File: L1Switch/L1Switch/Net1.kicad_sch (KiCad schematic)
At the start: 33 parts, among them J2 Conn_01x07_Male, U2 VSC8658

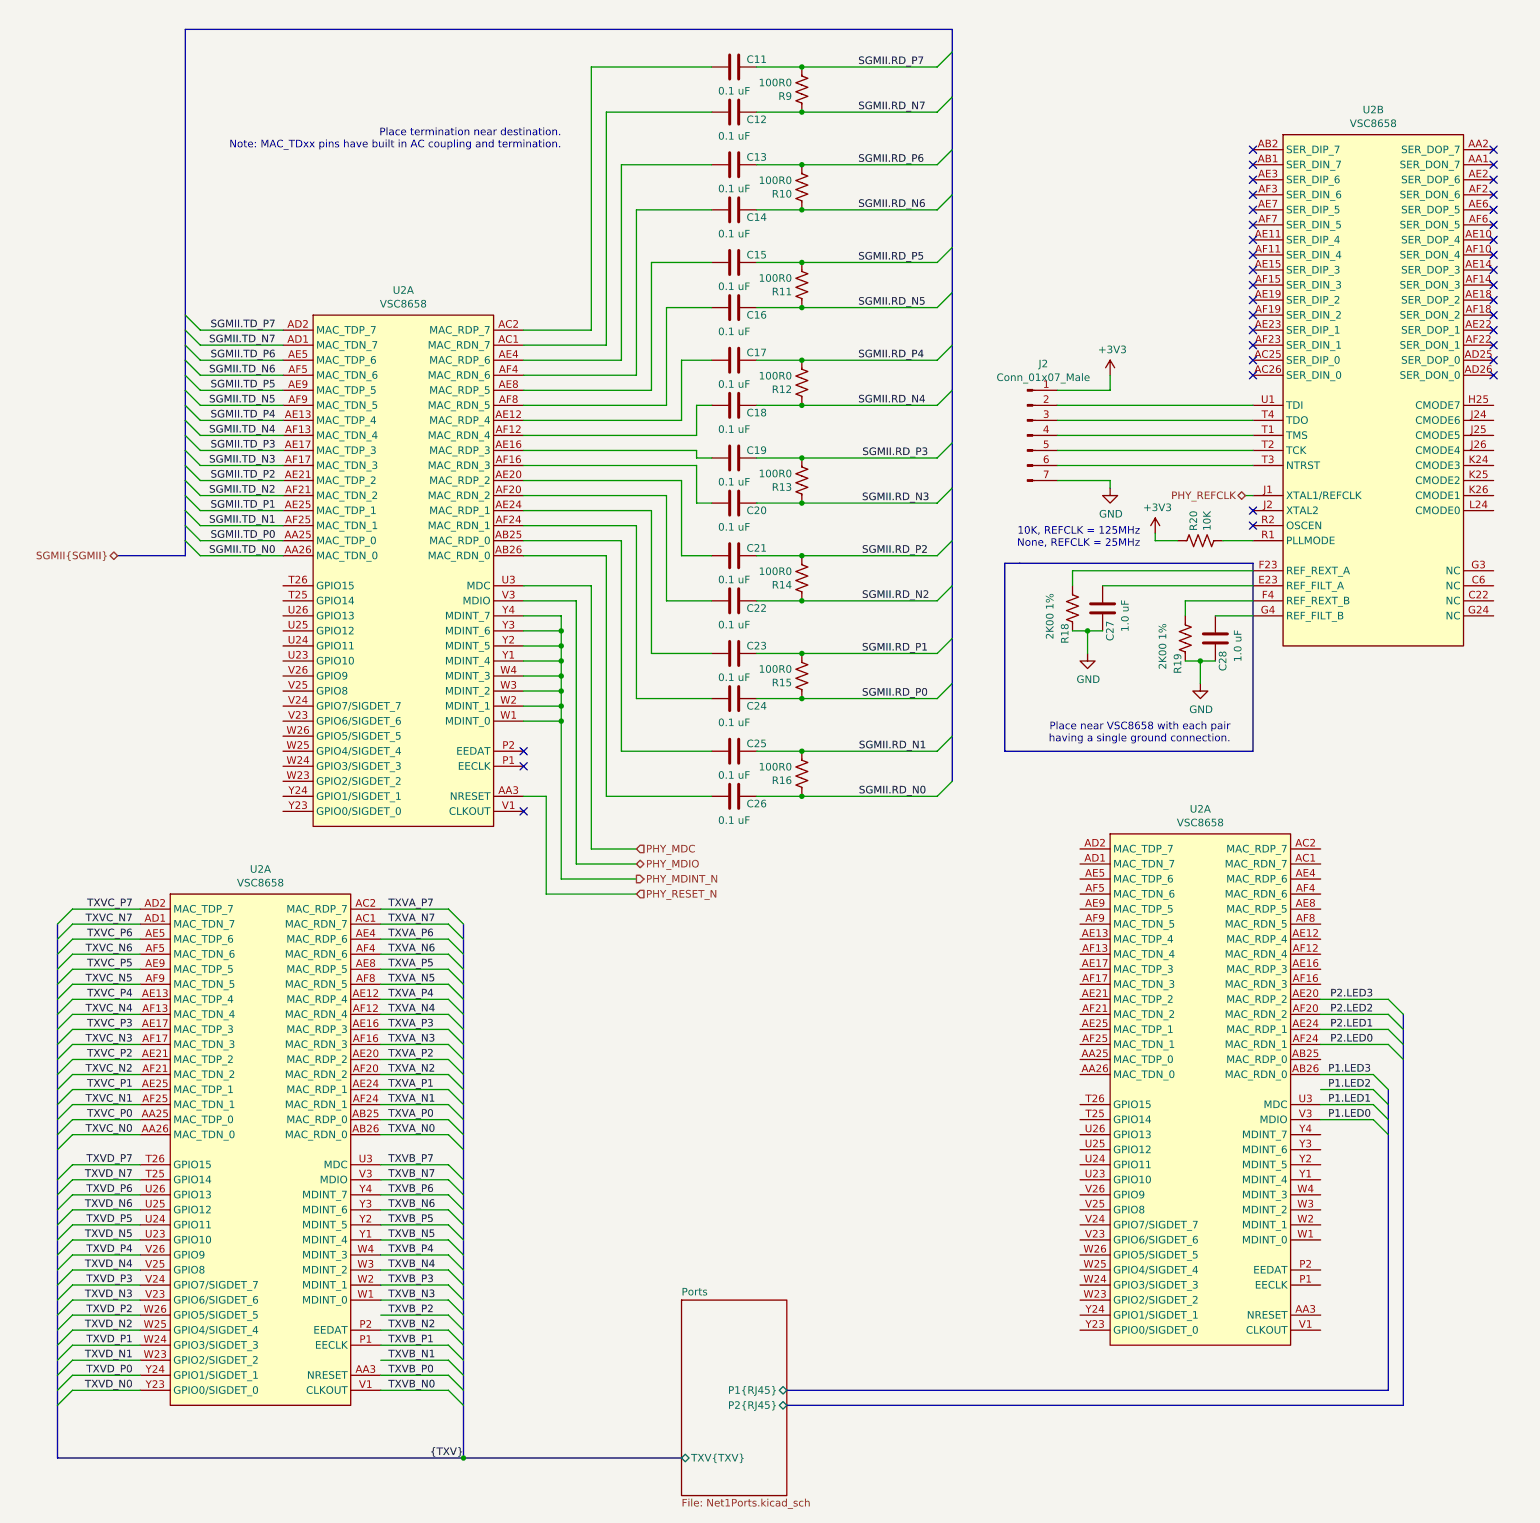
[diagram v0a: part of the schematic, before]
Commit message: Connect/route 8 ports to PHY.
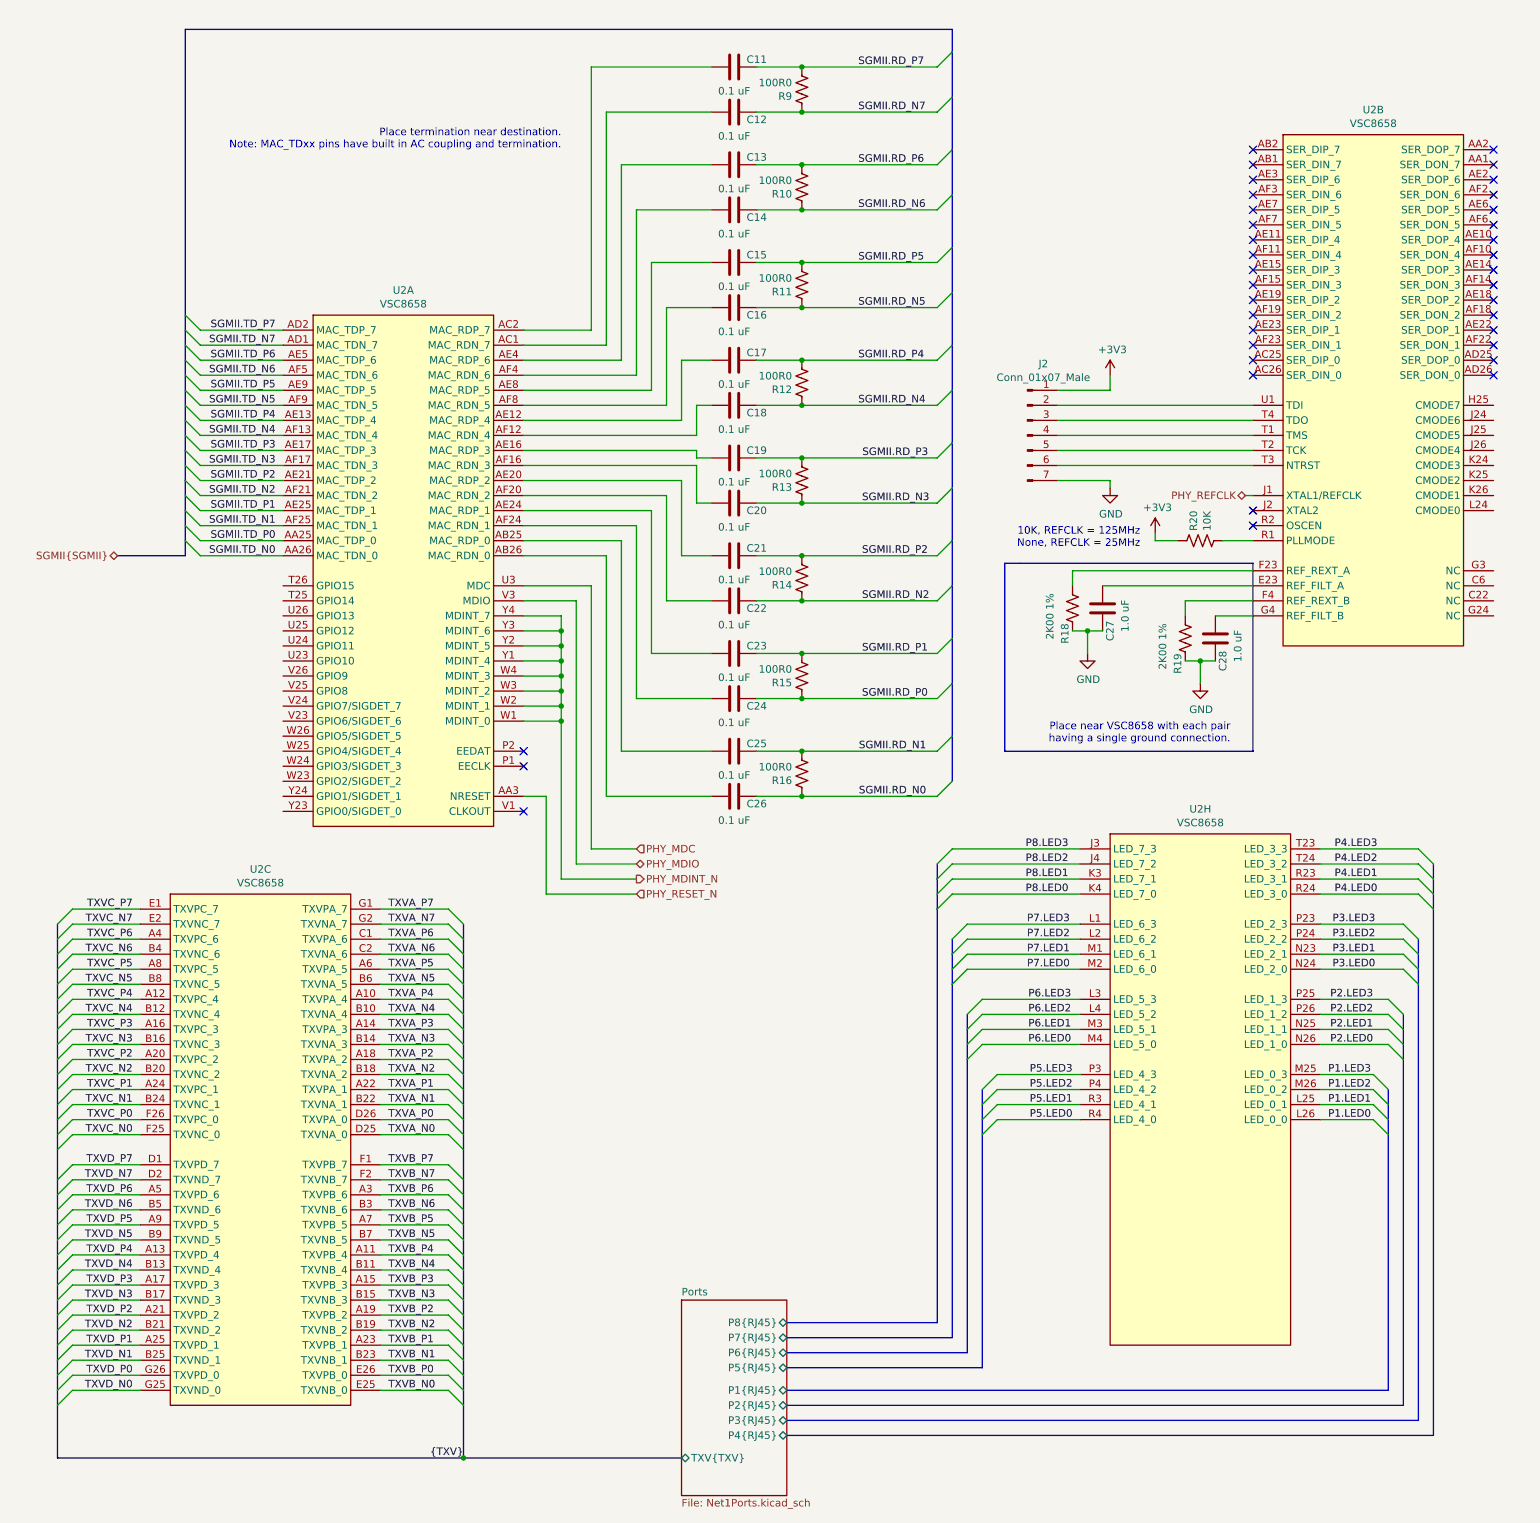
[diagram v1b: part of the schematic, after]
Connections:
- net P1.LED0: now also U2.L26 (LED_0_0); no longer U2.V3 (MDIO)
- net P1.LED1: now also U2.L25 (LED_0_1); no longer U2.U3 (MDC)
- net P1.LED2: now also U2.M26 (LED_0_2)
- net P1.LED3: now also U2.M25 (LED_0_3); no longer U2.AB26 (MAC_RDN_0)
- net P2.LED0: now also U2.N26 (LED_1_0); no longer U2.AF24 (MAC_RDN_1)
- net P2.LED1: now also U2.N25 (LED_1_1); no longer U2.AE24 (MAC_RDP_1)
- net P2.LED2: now also U2.P26 (LED_1_2); no longer U2.AF20 (MAC_RDN_2)
- net P2.LED3: now also U2.P25 (LED_1_3); no longer U2.AE20 (MAC_RDP_2)
- net TXVA_N0: now also U2.D25 (TXVNA_0); no longer U2.AB26 (MAC_RDN_0)
- net TXVA_N1: now also U2.B22 (TXVNA_1); no longer U2.AF24 (MAC_RDN_1)
- net TXVA_N2: now also U2.B18 (TXVNA_2); no longer U2.AF20 (MAC_RDN_2)
- net TXVA_N3: now also U2.B14 (TXVNA_3); no longer U2.AF16 (MAC_RDN_3)
- net TXVA_N4: now also U2.B10 (TXVNA_4); no longer U2.AF12 (MAC_RDN_4)
- net TXVA_N5: now also U2.B6 (TXVNA_5); no longer U2.AF8 (MAC_RDN_5)
- net TXVA_N6: now also U2.C2 (TXVNA_6); no longer U2.AF4 (MAC_RDN_6)
- net TXVA_N7: now also U2.G2 (TXVNA_7); no longer U2.AC1 (MAC_RDN_7)
- net TXVA_P0: now also U2.D26 (TXVPA_0); no longer U2.AB25 (MAC_RDP_0)
- net TXVA_P1: now also U2.A22 (TXVPA_1); no longer U2.AE24 (MAC_RDP_1)
- net TXVA_P2: now also U2.A18 (TXVPA_2); no longer U2.AE20 (MAC_RDP_2)
- net TXVA_P3: now also U2.A14 (TXVPA_3); no longer U2.AE16 (MAC_RDP_3)
- net TXVA_P4: now also U2.A10 (TXVPA_4); no longer U2.AE12 (MAC_RDP_4)
- net TXVA_P5: now also U2.A6 (TXVPA_5); no longer U2.AE8 (MAC_RDP_5)
- net TXVA_P6: now also U2.C1 (TXVPA_6); no longer U2.AE4 (MAC_RDP_6)
- net TXVA_P7: now also U2.G1 (TXVPA_7); no longer U2.AC2 (MAC_RDP_7)
- net TXVB_N0: now also U2.E25 (TXVNB_0); no longer U2.V1 (CLKOUT)
- net TXVB_N1: now also U2.B23 (TXVNB_1)
- net TXVB_N2: now also U2.B19 (TXVNB_2); no longer U2.P2 (EEDAT)
- net TXVB_N3: now also U2.B15 (TXVNB_3); no longer U2.W1 (MDINT_0)
- net TXVB_N4: now also U2.B11 (TXVNB_4); no longer U2.W3 (MDINT_2)
- net TXVB_N5: now also U2.B7 (TXVNB_5); no longer U2.Y1 (MDINT_4)
- net TXVB_N6: now also U2.B3 (TXVNB_6); no longer U2.Y3 (MDINT_6)
- net TXVB_N7: now also U2.F2 (TXVNB_7); no longer U2.V3 (MDIO)
- net TXVB_P0: now also U2.E26 (TXVPB_0); no longer U2.AA3 (NRESET)
- net TXVB_P1: now also U2.A23 (TXVPB_1); no longer U2.P1 (EECLK)
- net TXVB_P2: now also U2.A19 (TXVPB_2)
- net TXVB_P3: now also U2.A15 (TXVPB_3); no longer U2.W2 (MDINT_1)
- net TXVB_P4: now also U2.A11 (TXVPB_4); no longer U2.W4 (MDINT_3)
- net TXVB_P5: now also U2.A7 (TXVPB_5); no longer U2.Y2 (MDINT_5)
- net TXVB_P6: now also U2.A3 (TXVPB_6); no longer U2.Y4 (MDINT_7)
- net TXVB_P7: now also U2.F1 (TXVPB_7); no longer U2.U3 (MDC)
- net TXVC_N0: now also U2.F25 (TXVNC_0); no longer U2.AA26 (MAC_TDN_0)
- net TXVC_N1: now also U2.B24 (TXVNC_1); no longer U2.AF25 (MAC_TDN_1)
- net TXVC_N2: now also U2.B20 (TXVNC_2); no longer U2.AF21 (MAC_TDN_2)
- net TXVC_N3: now also U2.B16 (TXVNC_3); no longer U2.AF17 (MAC_TDN_3)
- net TXVC_N4: now also U2.B12 (TXVNC_4); no longer U2.AF13 (MAC_TDN_4)
- net TXVC_N5: now also U2.B8 (TXVNC_5); no longer U2.AF9 (MAC_TDN_5)
- net TXVC_N6: now also U2.B4 (TXVNC_6); no longer U2.AF5 (MAC_TDN_6)
- net TXVC_N7: now also U2.E2 (TXVNC_7); no longer U2.AD1 (MAC_TDN_7)
- net TXVC_P0: now also U2.F26 (TXVPC_0); no longer U2.AA25 (MAC_TDP_0)
- net TXVC_P1: now also U2.A24 (TXVPC_1); no longer U2.AE25 (MAC_TDP_1)
- net TXVC_P2: now also U2.A20 (TXVPC_2); no longer U2.AE21 (MAC_TDP_2)
- net TXVC_P3: now also U2.A16 (TXVPC_3); no longer U2.AE17 (MAC_TDP_3)
- net TXVC_P4: now also U2.A12 (TXVPC_4); no longer U2.AE13 (MAC_TDP_4)
- net TXVC_P5: now also U2.A8 (TXVPC_5); no longer U2.AE9 (MAC_TDP_5)
- net TXVC_P6: now also U2.A4 (TXVPC_6); no longer U2.AE5 (MAC_TDP_6)
- net TXVC_P7: now also U2.E1 (TXVPC_7); no longer U2.AD2 (MAC_TDP_7)
- net TXVD_N0: now also U2.G25 (TXVND_0); no longer U2.Y23 (GPIO0/SIGDET_0)
- net TXVD_N1: now also U2.B25 (TXVND_1); no longer U2.W23 (GPIO2/SIGDET_2)
- net TXVD_N2: now also U2.B21 (TXVND_2); no longer U2.W25 (GPIO4/SIGDET_4)
- net TXVD_N3: now also U2.B17 (TXVND_3); no longer U2.V23 (GPIO6/SIGDET_6)
- net TXVD_N4: now also U2.B13 (TXVND_4); no longer U2.V25 (GPIO8)
- net TXVD_N5: now also U2.B9 (TXVND_5); no longer U2.U23 (GPIO10)
- net TXVD_N6: now also U2.B5 (TXVND_6); no longer U2.U25 (GPIO12)
- net TXVD_N7: now also U2.D2 (TXVND_7); no longer U2.T25 (GPIO14)
- net TXVD_P0: now also U2.G26 (TXVPD_0); no longer U2.Y24 (GPIO1/SIGDET_1)
- net TXVD_P1: now also U2.A25 (TXVPD_1); no longer U2.W24 (GPIO3/SIGDET_3)
- net TXVD_P2: now also U2.A21 (TXVPD_2); no longer U2.W26 (GPIO5/SIGDET_5)
- net TXVD_P3: now also U2.A17 (TXVPD_3); no longer U2.V24 (GPIO7/SIGDET_7)
- net TXVD_P4: now also U2.A13 (TXVPD_4); no longer U2.V26 (GPIO9)
- net TXVD_P5: now also U2.A9 (TXVPD_5); no longer U2.U24 (GPIO11)
- net TXVD_P6: now also U2.A5 (TXVPD_6); no longer U2.U26 (GPIO13)
- net TXVD_P7: now also U2.D1 (TXVPD_7); no longer U2.T26 (GPIO15)
- new net P3.LED0: U2.N24 (LED_2_0)
- new net P3.LED1: U2.N23 (LED_2_1)
- new net P3.LED2: U2.P24 (LED_2_2)
- new net P3.LED3: U2.P23 (LED_2_3)
- new net P4.LED0: U2.R24 (LED_3_0)
- new net P4.LED1: U2.R23 (LED_3_1)
- new net P4.LED2: U2.T24 (LED_3_2)
- new net P4.LED3: U2.T23 (LED_3_3)
- new net P5.LED0: U2.R4 (LED_4_0)
- new net P5.LED1: U2.R3 (LED_4_1)
- new net P5.LED2: U2.P4 (LED_4_2)
- new net P5.LED3: U2.P3 (LED_4_3)
- new net P6.LED0: U2.M4 (LED_5_0)
- new net P6.LED1: U2.M3 (LED_5_1)
- new net P6.LED2: U2.L4 (LED_5_2)
- new net P6.LED3: U2.L3 (LED_5_3)
- new net P7.LED0: U2.M2 (LED_6_0)
- new net P7.LED1: U2.M1 (LED_6_1)
- new net P7.LED2: U2.L2 (LED_6_2)
- new net P7.LED3: U2.L1 (LED_6_3)
- new net P8.LED0: U2.K4 (LED_7_0)
- new net P8.LED1: U2.K3 (LED_7_1)
- new net P8.LED2: U2.J4 (LED_7_2)
- new net P8.LED3: U2.J3 (LED_7_3)
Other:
- sheet Ports ports: added P3{RJ45}, P4{RJ45}, P5{RJ45}, P6{RJ45}, P7{RJ45}, P8{RJ45}; removed none
